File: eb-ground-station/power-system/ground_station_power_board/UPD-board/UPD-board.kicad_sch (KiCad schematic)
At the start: 97 parts, among them J1 Conn_01x04, J10 PI 1827486, J2 PC 1720806, J3 Conn_01x03, J4 Conn_01x03, J5 Conn_01x03, J6 Conn_01x03, J7 PI 1924143, J8 PI 1827923, J9 PI 1827486, Q21 SUD50P08-25L-E3, Q22 SUD50P08-25L-E3, U1 MAX7310ATE, U2 MAX7310ATE, U3 MAX7310ATE, U4 MCP9808, U5 ADS1115IDGS, U6 UA78M33, U7 U_RasPi_40pin

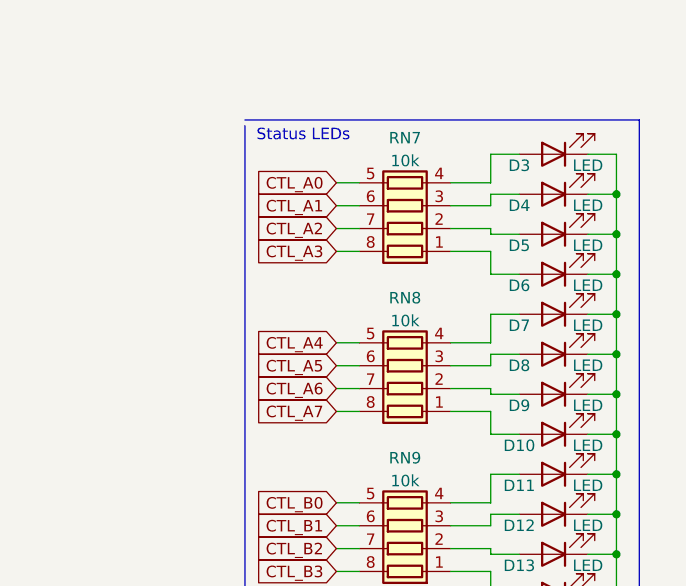
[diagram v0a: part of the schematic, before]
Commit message: Upgrading Bank A to 16A
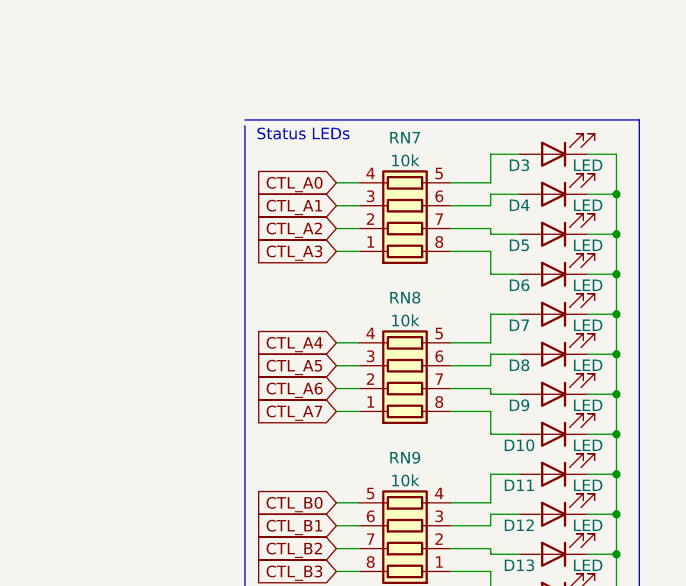
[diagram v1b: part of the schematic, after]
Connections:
- net CTL_A0: now also RN7.4 (R4.1); no longer RN7.5 (R4.2)
- net CTL_A1: now also RN7.3 (R3.1); no longer RN7.6 (R3.2)
- net CTL_A2: now also RN7.2 (R2.1); no longer RN7.7 (R2.2)
- net CTL_A3: now also RN7.1 (R1.1); no longer RN7.8 (R1.2)
- net CTL_A4: now also RN8.4 (R4.1); no longer RN8.5 (R4.2)
- net CTL_A5: now also RN8.3 (R3.1); no longer RN8.6 (R3.2)
- net CTL_A6: now also RN8.2 (R2.1); no longer RN8.7 (R2.2)
- net CTL_A7: now also RN8.1 (R1.1); no longer RN8.8 (R1.2)
- net at D9.2 (A): now also RN8.7 (R2.2); no longer RN8.2 (R2.1)
- net at D6.2 (A): now also RN7.8 (R1.2); no longer RN7.1 (R1.1)
- net at D3.2 (A): now also RN7.5 (R4.2); no longer RN7.4 (R4.1)
- net at D10.2 (A): now also RN8.8 (R1.2); no longer RN8.1 (R1.1)
- net at D8.2 (A): now also RN8.6 (R3.2); no longer RN8.3 (R3.1)
- net at D7.2 (A): now also RN8.5 (R4.2); no longer RN8.4 (R4.1)
- net at D5.2 (A): now also RN7.7 (R2.2); no longer RN7.2 (R2.1)
- net at D4.2 (A): now also RN7.6 (R3.2); no longer RN7.3 (R3.1)
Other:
- moved on the sheet: RN7, RN8
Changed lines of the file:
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@@
     (pin "2")
   )
-  (symbol (lib_id "Device:R_Pack04") (at 390.525 179.705 90) (unit 1)
+  (symbol (lib_id "Device:R_Pack04") (at 390.525 179.705 270) (mirror x) (unit 1)
     (in_bom yes) (on_board yes) (fields_autoplaced)
     (property "Reference" "RN8" (id 0) (at 390.525 172.1952 90))
@@
     (pin "9")
   )
-  (symbol (lib_id "Device:R_Pack04") (at 390.525 161.925 90) (unit 1)
+  (symbol (lib_id "Device:R_Pack04") (at 390.525 161.925 270) (mirror x) (unit 1)
     (in_bom yes) (on_board yes) (fields_autoplaced)
     (property "Reference" "RN7" (id 0) (at 390.525 154.4152 90))
@@
       (reference "#PWR052") (unit 1) (value "GND") (footprint "")
     )
-    (path "/3a1c5476-bb6a-4918-80d3-82e1846e9dbb/85da5a9a-53e7-44e1-9190-755e9e079bd5"
-      (reference "#PWR053") (unit 1) (value "+12V") (footprint "")
-    )
-    (path "/3a1c5476-bb6a-4918-80d3-82e1846e9dbb/e27fc768-1691-4e3e-8d81-91f753d218c6"
-      (reference "#PWR054") (unit 1) (value "GND") (footprint "")
-    )
     (path "/3a1c5476-bb6a-4918-80d3-82e1846e9dbb/61add8aa-9a72-491c-a55f-f7288f365b0c"
       (reference "#PWR055") (unit 1) (value "+12V") (footprint "")
@@
       (reference "#PWR077") (unit 1) (value "+12V") (footprint "")
     )
-    (path "/3a1c5476-bb6a-4918-80d3-82e1846e9dbb/a8e628b5-7a01-4a17-9d93-9bfb84a02532"
-      (reference "#PWR078") (unit 1) (value "GND") (footprint "")
-    )
     (path "/3a1c5476-bb6a-4918-80d3-82e1846e9dbb/b074fd18-c4f8-4fa5-8a7e-0ccc32c94a07"
       (reference "#PWR079") (unit 1) (value "+12V") (footprint "")
@@
       (reference "#PWR0100") (unit 1) (value "GND") (footprint "")
     )
-    (path "/3a1c5476-bb6a-4918-80d3-82e1846e9dbb/42dac526-eded-494e-8413-081ad2941a0d"
-      (reference "#PWR0101") (unit 1) (value "+12V") (footprint "")
-    )
-    (path "/3a1c5476-bb6a-4918-80d3-82e1846e9dbb/efc32ce5-b38c-4093-86bb-0e70e1cedc40"
-      (reference "#PWR0102") (unit 1) (value "GND") (footprint "")
-    )
     (path "/3a1c5476-bb6a-4918-80d3-82e1846e9dbb/c050cfc6-bc7c-480f-94e2-7557f67fb12b"
       (reference "#PWR0103") (unit 1) (value "GND") (footprint "")
@@
       (reference "#PWR0108") (unit 1) (value "+5V") (footprint "")
     )
-    (path "/3a1c5476-bb6a-4918-80d3-82e1846e9dbb/504cb964-7d48-45d9-8ef4-39473efc87f8"
-      (reference "#PWR0109") (unit 1) (value "+12V") (footprint "")
-    )
-    (path "/3a1c5476-bb6a-4918-80d3-82e1846e9dbb/9e165268-ae18-40cb-928f-62951ba1f45e"
-      (reference "#PWR0110") (unit 1) (value "GND") (footprint "")
-    )
     (path "/3a1c5476-bb6a-4918-80d3-82e1846e9dbb/84c28457-6e31-4c65-8539-377808b3bd60"
       (reference "#PWR0111") (unit 1) (value "GND") (footprint "")
@@
       (reference "U7") (unit 1) (value "U_RasPi_40pin") (footprint "Connector_IDC:IDC-Header_2x20_P2.54mm_Vertical")
     )
-    (path "/3a1c5476-bb6a-4918-80d3-82e1846e9dbb/b28562c4-ee1d-4560-bebd-4f57e0618265"
-      (reference "U8") (unit 1) (value "TC4427") (footprint "Package_SO:MSOP-8_3x3mm_P0.65mm")
-    )
     (path "/3a1c5476-bb6a-4918-80d3-82e1846e9dbb/281d453c-a5c9-44fc-8cf2-591a30a18602"
       (reference "U9") (unit 1) (value "TC4427") (footprint "Package_SO:MSOP-8_3x3mm_P0.65mm")
@@
       (reference "U12") (unit 1) (value "TC4427") (footprint "Package_SO:MSOP-8_3x3mm_P0.65mm")
     )
-    (path "/3a1c5476-bb6a-4918-80d3-82e1846e9dbb/7d43d709-b2e3-4b83-b9f2-291b8278a056"
-      (reference "U13") (unit 1) (value "TC4427") (footprint "Package_SO:MSOP-8_3x3mm_P0.65mm")
-    )
     (path "/3a1c5476-bb6a-4918-80d3-82e1846e9dbb/3a997cb8-dfd3-4377-9272-2b6483276523"
       (reference "U14") (unit 1) (value "TC4427") (footprint "Package_SO:MSOP-8_3x3mm_P0.65mm")
@@
       (reference "U17") (unit 1) (value "TC4427") (footprint "Package_SO:MSOP-8_3x3mm_P0.65mm")
     )
-    (path "/3a1c5476-bb6a-4918-80d3-82e1846e9dbb/ff90f230-e14e-467f-8a56-1ee4434f31c3"
-      (reference "U18") (unit 1) (value "TC4427") (footprint "Package_SO:MSOP-8_3x3mm_P0.65mm")
-    )
-    (path "/3a1c5476-bb6a-4918-80d3-82e1846e9dbb/20a49954-d3bd-4355-bfa3-4aad99cddc30"
-      (reference "U19") (unit 1) (value "TC4427") (footprint "Package_SO:MSOP-8_3x3mm_P0.65mm")
-    )
-  )
+  )

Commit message: Silkscreen almost done
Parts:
- added D3: LED, LED_SMD:LED_0603_1608Metric, symbol Device:LED
- added J11: Conn_02x02_Odd_Even, Connector_PinHeader_2.54mm:PinHeader_2x02_P2.54mm_Vertical, symbol Connector_Generic:Conn_02x02_Odd_Even
- added R27, R28: 4k7, Resistor_SMD:R_0603_1608Metric, symbol Device:R
- added R8: 1500, Resistor_SMD:R_0603_1608Metric, symbol Device:R
- added TP1, TP2, TP3: TestPoint, oresat-footprints:TestPoint_Pad_1.5x1.5mm, symbol Connector:TestPoint
- renumbered D9 to D10, D10 to D11, D11 to D12, D12 to D13, D13 to D14, D14 to D15, D15 to D16, D16 to D17, D17 to D18, D18 to D19, D19 to D20, D20 to D21, D21 to D22, D22 to D23, D23 to D24, D24 to D25, D25 to D26, D26 to D27, D3 to D4, D4 to D5, D5 to D6, D6 to D7, D7 to D8, D8 to D9
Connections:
- net +12V: now also TP1.1
- net +3V3: now also D3.2 (A), R27.1, R28.1, TP3.1; no longer JP1.3 (B), JP2.3 (B), JP3.3 (B), JP4.1 (A), JP5.3 (B), JP6.3 (B), JP7.3 (B), JP8.1 (A), JP9.3 (B)
- net +5V: now also TP2.1
- net ADC_RDY: now also J11.4 (Pin_4), R28.2
- net GND: now also J11.1 (Pin_1), R8.1; no longer JP1.1 (A), JP2.1 (A), JP3.1 (A), JP4.3 (B), JP5.1 (A), JP6.1 (A), JP7.1 (A), JP8.3 (B), JP9.1 (A)
- net SCL: now also JP1.1 (A), JP2.1 (A), JP3.1 (A), JP4.3 (B), JP5.1 (A), JP6.1 (A), JP7.1 (A), JP8.3 (B), JP9.1 (A)
- net SDA: now also JP1.3 (B), JP2.3 (B), JP3.3 (B), JP4.1 (A), JP5.3 (B), JP6.3 (B), JP7.3 (B), JP8.1 (A), JP9.3 (B)
- net TMP_ALERT: now also J11.3 (Pin_3), R27.2
- net ~{IO_RESET}: now also J11.2 (Pin_2)
- new net: D3.1 (K), R8.2
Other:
- note added: "0"
- note added: "0011{A2}{A1}{A0}"
- note added: "0x18-0x1F"
- note added: "1"
- note added: "Alt. ADDR: 0x49"
- note added: "Def: 0x20"
- note added: "Def: 0x21"
- note added: "Def: 0x22"
- note added: "Populate R4/5 to use UART2 as I2C0"
- note removed: "Populate these to use UART2 as I2C0"
- moved on the sheet: C1, C2, C3, C4, C5, C9, FB1, FB2, JP1, JP10, JP11, JP12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

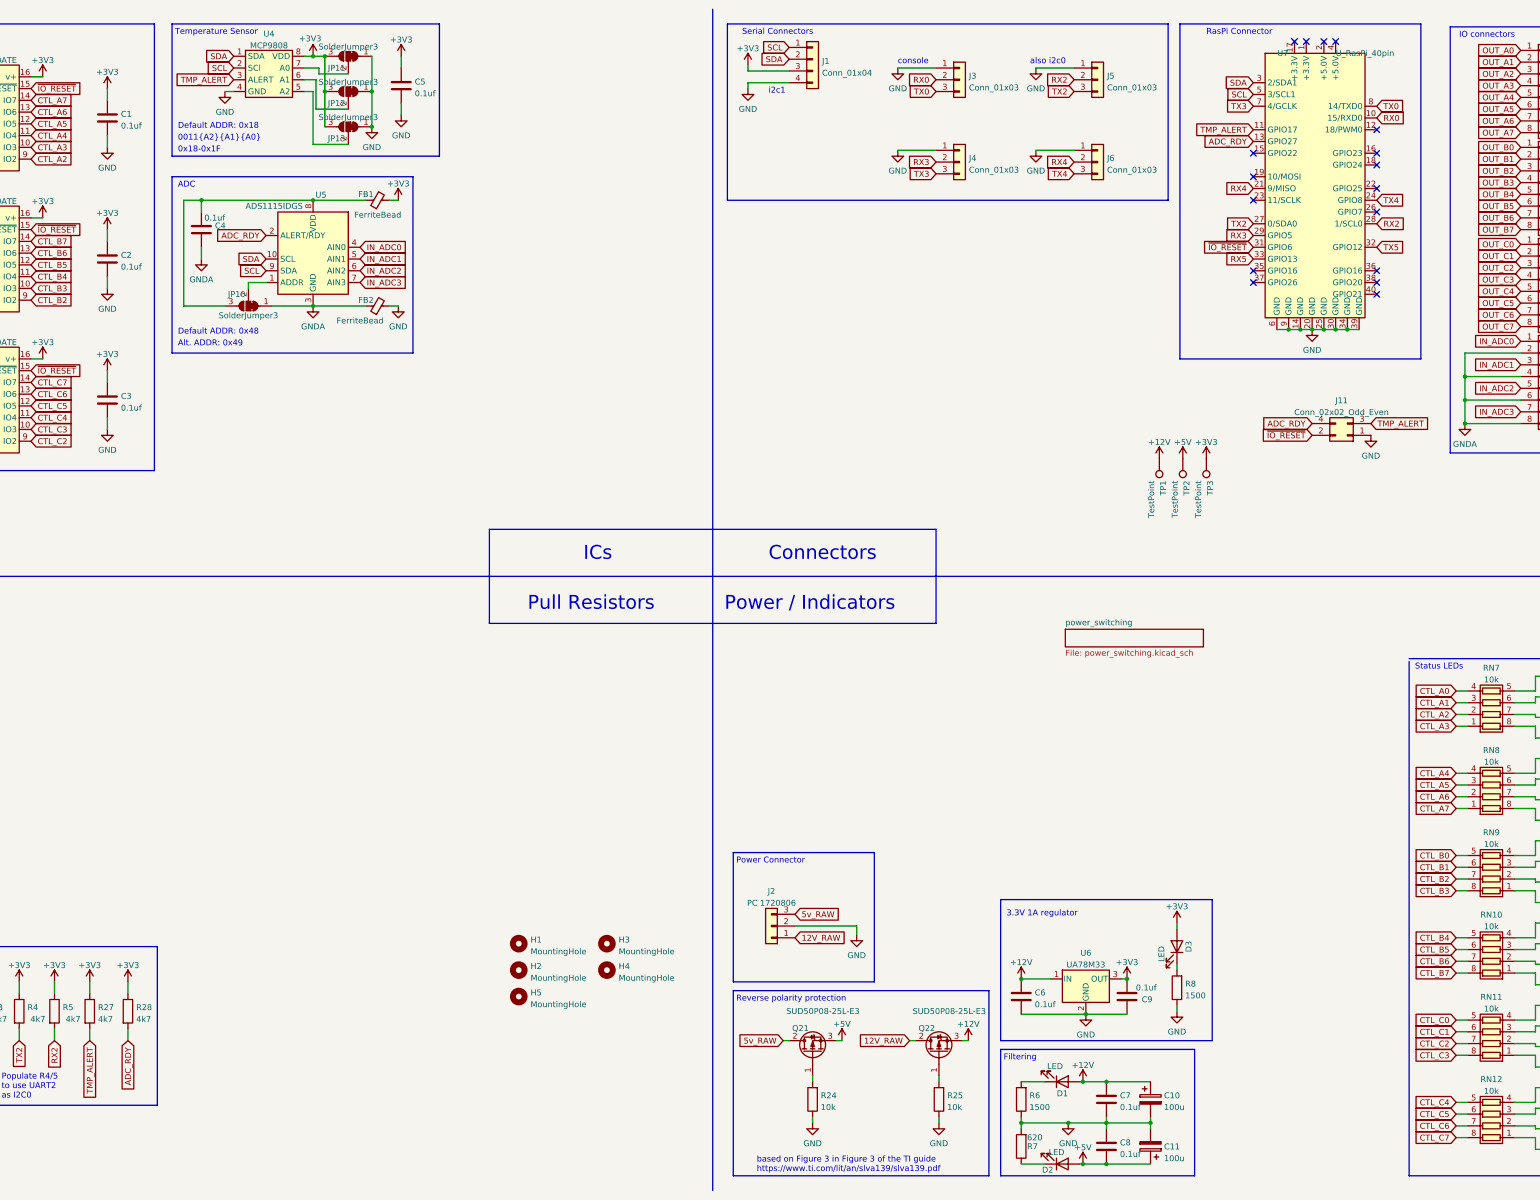
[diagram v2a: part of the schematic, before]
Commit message: Made new drawings and renders
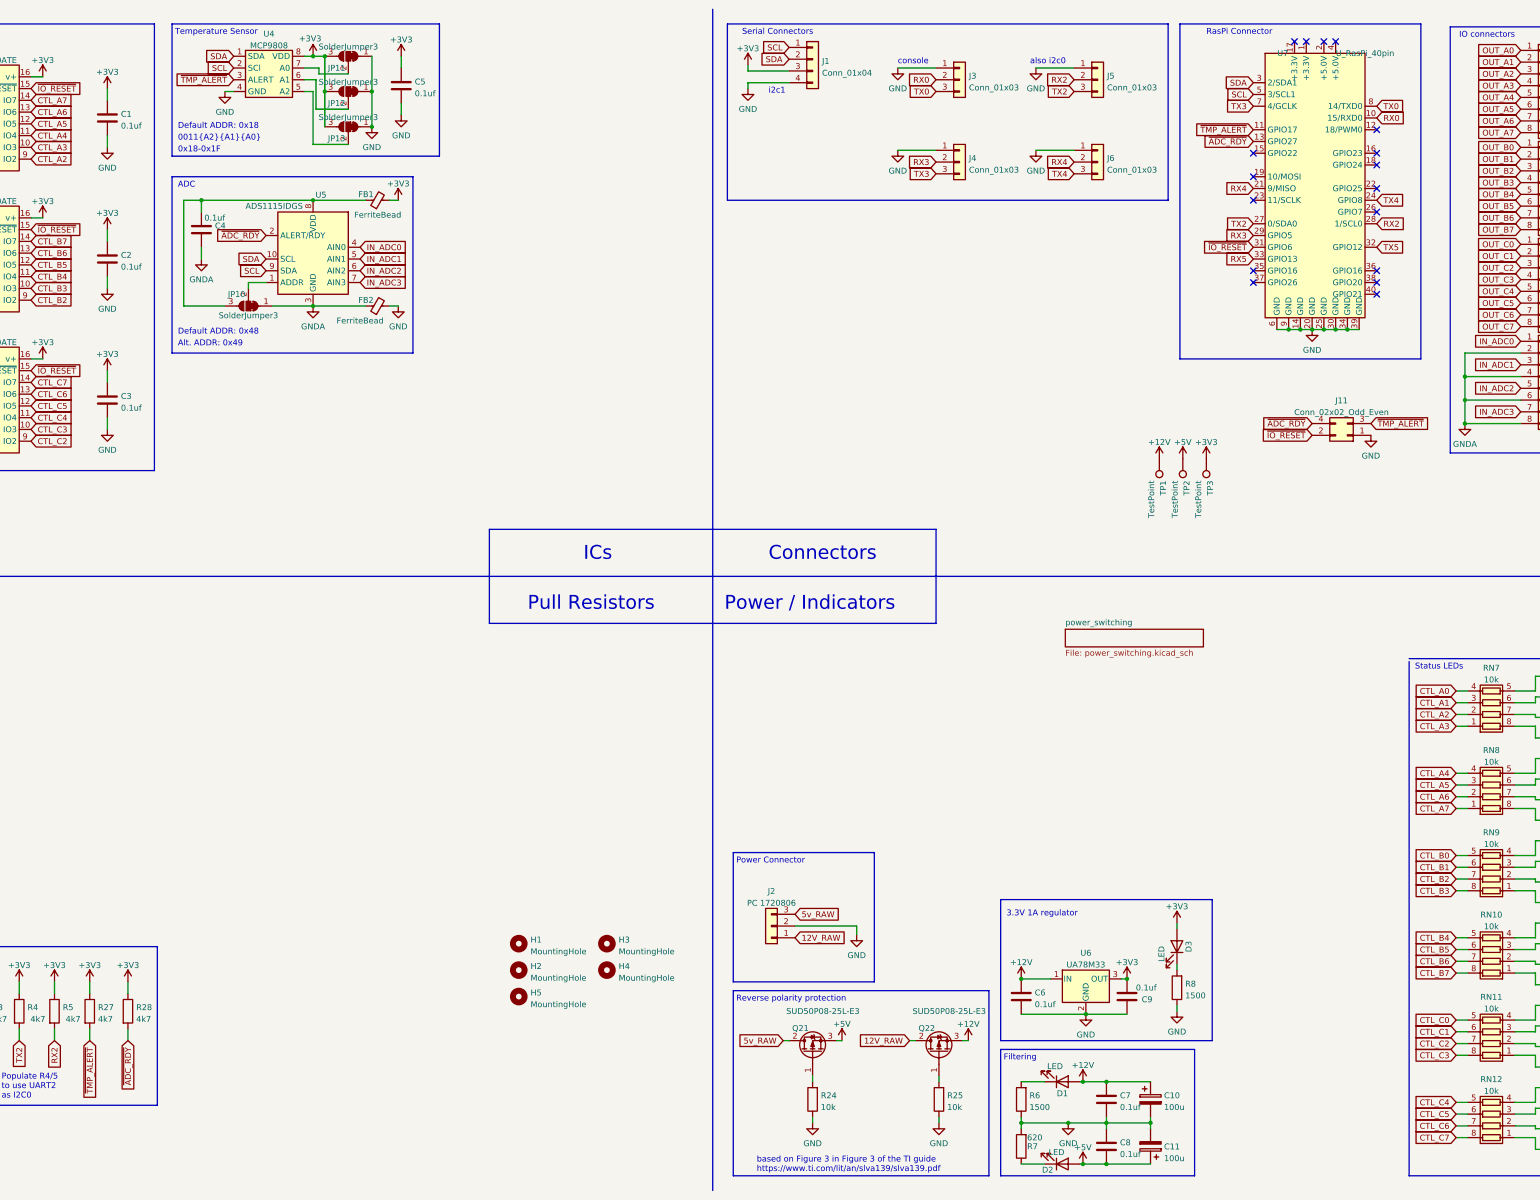
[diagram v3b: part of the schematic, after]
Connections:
- net ADC_RDY renamed ~{ADC_RDY}
- net TMP_ALERT renamed ~{TMP_ALERT}
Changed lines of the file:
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@@
     )
   )
-  (global_label "ADC_RDY" (shape input) (at 125.73 60.96 180) (fields_autoplaced)
+  (global_label "~{ADC_RDY}" (shape input) (at 125.73 60.96 180) (fields_autoplaced)
     (effects (font (size 1.27 1.27)) (justify right))
     (property "Intersheet References" "${INTERSHEET_REFS}" (id 0) (at 115.0921 60.8806 0)
@@
     )
   )
-  (global_label "TMP_ALERT" (shape input) (at 87.63 234.95 270) (fields_autoplaced)
+  (global_label "~{TMP_ALERT}" (shape input) (at 87.63 234.95 270) (fields_autoplaced)
     (effects (font (size 1.27 1.27)) (justify right))
     (property "Intersheet References" "${INTERSHEET_REFS}" (id 0) (at 87.5506 247.5231 90)
@@
     )
   )
-  (global_label "ADC_RDY" (shape input) (at 339.09 40.64 180) (fields_autoplaced)
+  (global_label "~{ADC_RDY}" (shape input) (at 339.09 40.64 180) (fields_autoplaced)
     (effects (font (size 1.27 1.27)) (justify right))
     (property "Intersheet References" "${INTERSHEET_REFS}" (id 0) (at 328.4521 40.5606 0)
@@
     )
   )
-  (global_label "ADC_RDY" (shape input) (at 351.79 101.6 180) (fields_autoplaced)
+  (global_label "~{ADC_RDY}" (shape input) (at 351.79 101.6 180) (fields_autoplaced)
     (effects (font (size 1.27 1.27)) (justify right))
     (property "Intersheet References" "${INTERSHEET_REFS}" (id 0) (at 341.1521 101.5206 0)
@@
     )
   )
-  (global_label "TMP_ALERT" (shape input) (at 364.49 101.6 0) (fields_autoplaced)
-    (effects (font (size 1.27 1.27)) (justify left))
-    (property "Intersheet References" "${INTERSHEET_REFS}" (id 0) (at 377.0631 101.6794 0)
+  (global_label "~{TMP_ALERT}" (shape input) (at 364.49 101.6 0) (fields_autoplaced)
+    (effects (font (size 1.27 1.27)) (justify left))
+    (property "Intersheet References" "${INTERSHEET_REFS}" (id 0) (at 377.0631 101.5206 0)
       (effects (font (size 1.27 1.27)) (justify left) hide)
     )
@@
     )
   )
-  (global_label "TMP_ALERT" (shape input) (at 118.745 27.305 180) (fields_autoplaced)
+  (global_label "~{TMP_ALERT}" (shape input) (at 118.745 27.305 180) (fields_autoplaced)
     (effects (font (size 1.27 1.27)) (justify right))
     (property "Intersheet References" "${INTERSHEET_REFS}" (id 0) (at 106.1719 27.2256 0)
@@
     )
   )
-  (global_label "TMP_ALERT" (shape input) (at 339.09 38.1 180) (fields_autoplaced)
+  (global_label "~{TMP_ALERT}" (shape input) (at 339.09 38.1 180) (fields_autoplaced)
     (effects (font (size 1.27 1.27)) (justify right))
     (property "Intersheet References" "${INTERSHEET_REFS}" (id 0) (at 326.5169 38.0206 0)
@@
     )
   )
-  (global_label "ADC_RDY" (shape input) (at 95.885 234.95 270) (fields_autoplaced)
+  (global_label "~{ADC_RDY}" (shape input) (at 95.885 234.95 270) (fields_autoplaced)
     (effects (font (size 1.27 1.27)) (justify right))
     (property "Intersheet References" "${INTERSHEET_REFS}" (id 0) (at 95.8056 245.5879 90)

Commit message: Fixed issues discovered during the design review
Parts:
- removed RN1, RN2, RN3, RN4, RN5, RN6: 10k, Resistor_SMD:R_Array_Convex_4x0603, symbol Device:R_Pack04
- added C20: 100u, Capacitor_SMD:CP_Elec_6.3x5.9, symbol Device:C_Polarized
- added FB3: FerriteBead, oresat-footprints:1206-or-0805, symbol Device:FerriteBead_Small
- added J12: Conn_01x05, Connector_PinHeader_2.54mm:PinHeader_1x05_P2.54mm_Vertical, symbol Connector_Generic:Conn_01x05
- added U13, U18, U19, U20, U21, U22, U8: dot_small, symbol graphics:dot_small
- FB1: DPN (none) -> 1292-WLBD2012HCU310THTR-ND; MPN (none) -> WLBD2012HCU310TH; Mfr (none) -> Walsin Technology Corporation
- FB2: value FerriteBead -> Link
- R1, R2, R24, R25, R27, R28, R3, R4, R5, R6, R7, R8: symbol Device:R -> Device:R_US
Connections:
- net +12V: now also FB3.1; no longer C6.1, U6.1 (IN)
- net +3V3: now also C20.1
- net GND: now also C20.2
- net GNDA: now also J12.1 (Pin_1)
- net IN_ADC0: now also J12.5 (Pin_5)
- net IN_ADC1: now also J12.4 (Pin_4)
- net IN_ADC2: now also J12.3 (Pin_3)
- net IN_ADC3: now also J12.2 (Pin_2)
- net 5v_RAW renamed 5V_RAW
- new net: C6.1, FB3.2, U6.1 (IN)
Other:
- note added: "1 0"
- note added: "12V"
- note added: "12V @ 16A 5V @ 16A"
- note added: "3.3V"
- note added: "3.3V @ 1A out"
- note added: "3.3V regulator"
- note added: "5V"
- note added: "CTL_A[0:7]"
- note added: "CTL_B[0:7]"
- note added: "CTL_C[0:7]"
- note added: "Future note: Consider using gnd/vcc for address"
- note added: "IN_ADC[0:3]"
- note added: "OUT_A[0:7]"
- note added: "OUT_B[0:7]"
- note added: "OUT_C[0:7]"
- note added: "Output LEDs"
- note added: "Populate FB2 with a 0 ohm link"
- note added: "Power Input"
- note added: "Power LEDs"
- note added: "Q21 & Q22 for reverse polarity protection based on Figure 3 of the TI guide https://www.ti.com/lit/an/slva139/slva139.pdf"
- note added: "RasPi"
- note added: "Test Points"
- note added: "UART0"
- note added: "UART2"
- note added: "UART3"
- note added: "UART4"
- note added: "caution: beware of ground loops when connecting to AGND"
- note added: "gnda"
- note added: "i2c"
- note added: "~{ADC_READY}"
- note added: "~{IO_RESET}"
- note added: "~{TMP_ALERT}"
- note removed: "3.3V 1A regulator"
- note removed: "Connectors"
- note removed: "Filtering"
- note removed: "ICs"
- note removed: "IO Pulldowns"
- note removed: "Power / Indicators"
- note removed: "Power Connector"
- note removed: "Pull Resistors"
- note removed: "RasPi Connector"
- note removed: "Reverse polarity protection"
- note removed: "Signal Pullups"
- note removed: "Status LEDs"
- note removed: "based on Figure 3 in Figure 3 of the TI guide https://www.ti.com/lit/an/slva139/slva139.pdf"
- moved on the sheet: C1, C10, C11, C2, C3, C4, C5, C6, C7, C8, C9, D1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
